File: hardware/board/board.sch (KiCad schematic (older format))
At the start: 32 parts, among them J1 MIC_SOCKET, J2 MIC_SOCKET, J3 MIC_SOCKET, P1 Power, P2 Analog, P3 Digital, P4 Digital, P5 CONN_01X01, P6 CONN_01X01, P7 CONN_01X01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

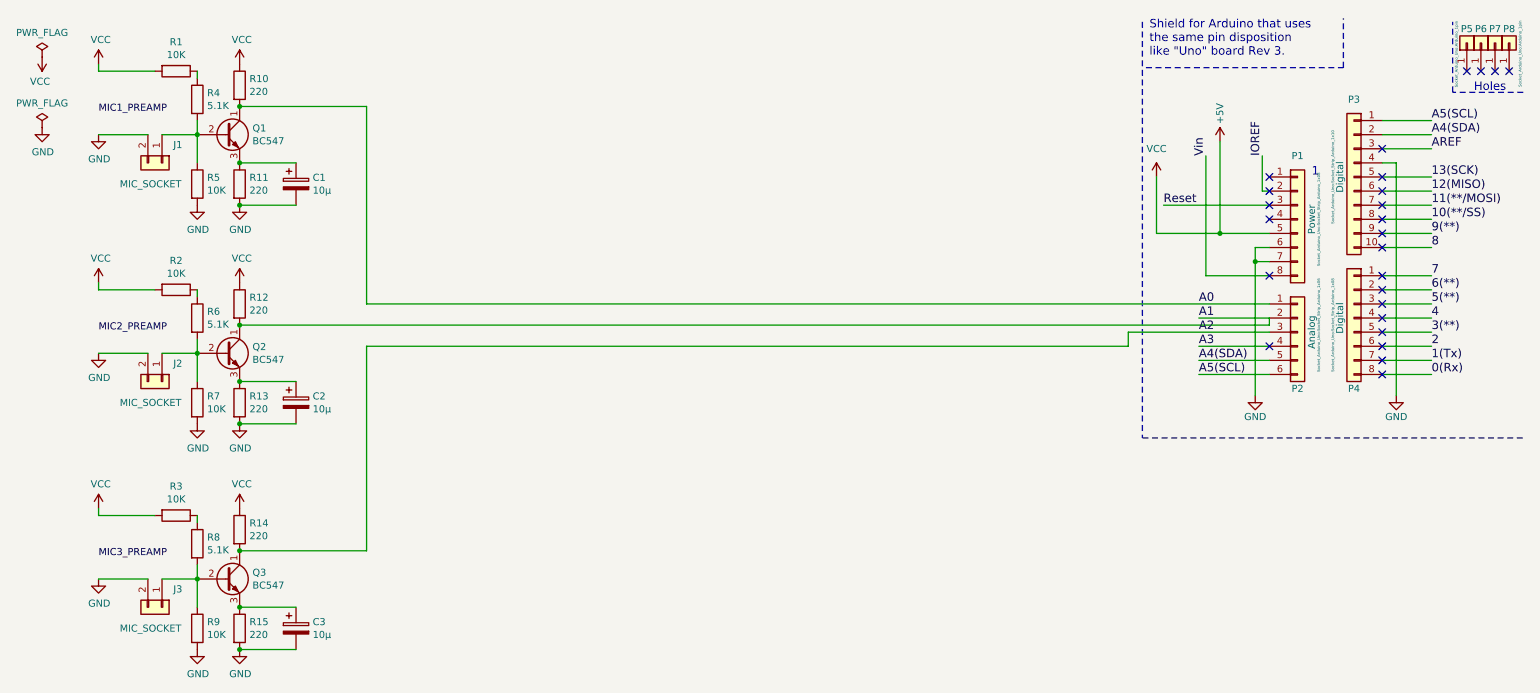
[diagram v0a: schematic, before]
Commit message: New microphone inputs sockets
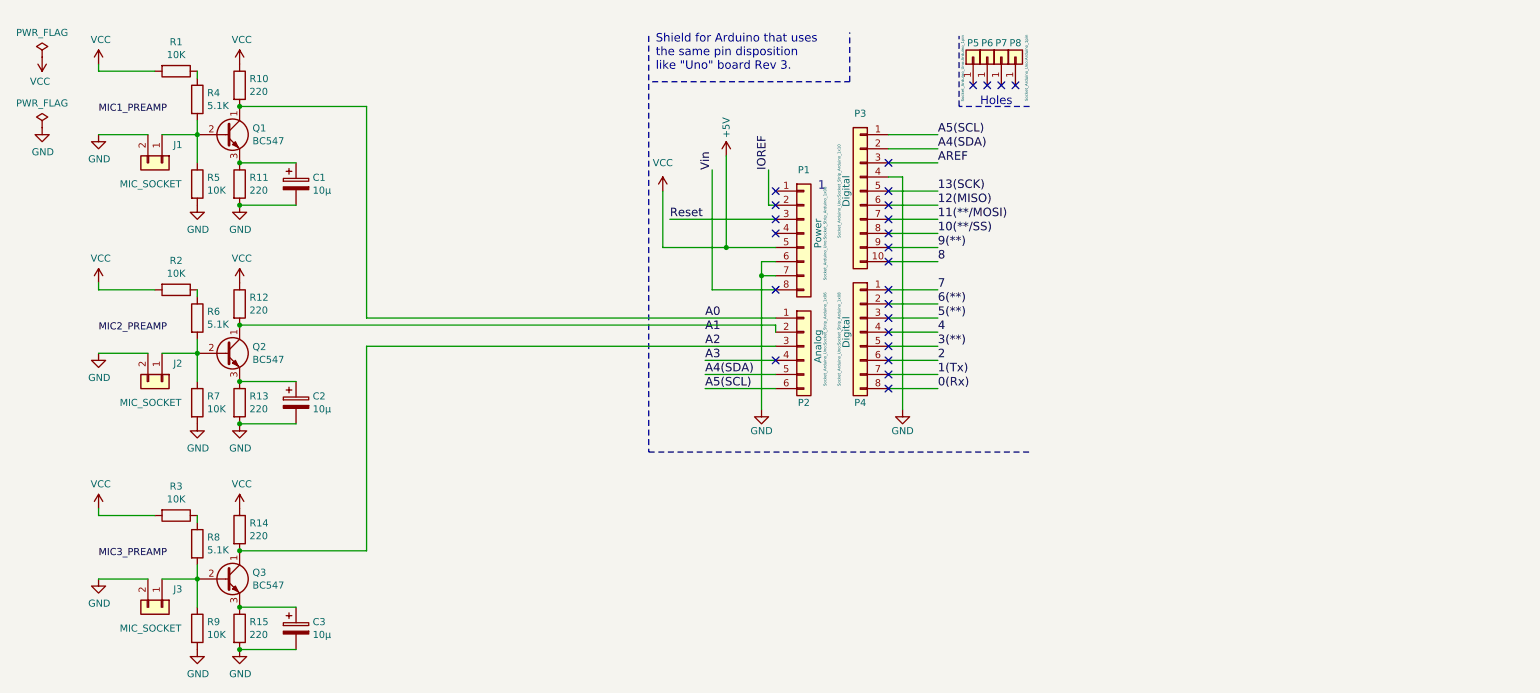
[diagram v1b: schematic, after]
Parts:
- J1, J2, J3: footprint Connector_Pin:Pin_D1.0mm_L10.0mm -> Connector_PinSocket_1.00mm:PinSocket_1x02_P1.00mm_Vertical
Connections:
- net A1: no longer P2.2 (Pin_2), Q2.1 (C), R12.2
- new net: P2.2 (Pin_2), Q2.1 (C), R12.2
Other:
- moved on the sheet: P1, P2, P3, P4, P5, P6, P7, P8
